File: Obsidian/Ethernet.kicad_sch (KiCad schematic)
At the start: 41 parts, among them J3 BELFUSE_0826-1G1T-43-F, U7 RTL8211F-CG, Y4 XTAL_25MHZ_EPSON_TSX-3225_25.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

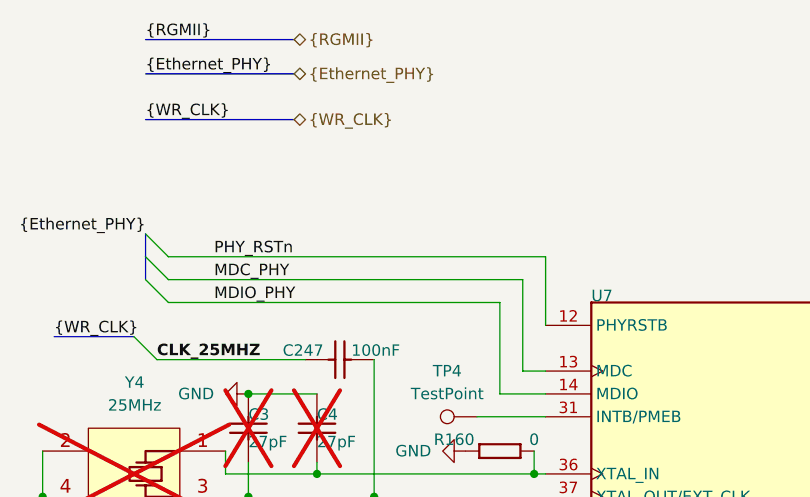
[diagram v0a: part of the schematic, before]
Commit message: adding lcsc reference for PMOD
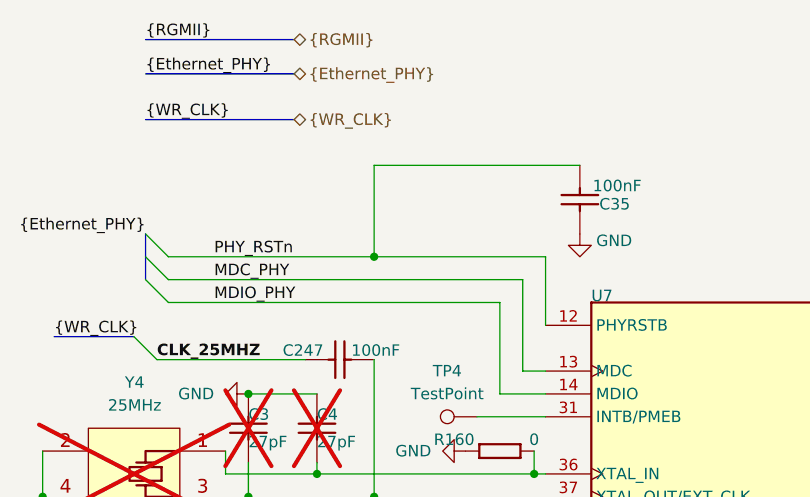
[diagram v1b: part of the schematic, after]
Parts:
- added C35: CC0402_100NF_50V_10%_X7R, Capacitor_SMD:C_0402_1005Metric, symbol Library_Symbol:CC0402_100NF_50V_10%_X7R
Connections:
- net GND: now also C35.2
- net PHY_RSTn: now also C35.1

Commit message: update LCSC reference, and OFFSET rotation for JLCPCB
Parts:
- C35: footprint Capacitor_SMD:C_0402_1005Metric -> Footprint:CAPC1005X55N
- J3: LCSC C6776261 -> C6062830
- L1: LCSC C6685204 -> C48945746
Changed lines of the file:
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@@
 			)
 		)
-		(property "Footprint" "Capacitor_SMD:C_0402_1005Metric"
+		(property "Footprint" "Footprint:CAPC1005X55N"
 			(at 73.152 34.29 0)
 			(effects
@@
 			)
 		)
-		(property "LCSC" "C6776261"
+		(property "LCSC" "C6062830"
 			(at 227.33 102.87 0)
 			(effects
@@
 			)
 		)
-		(property "LCSC" "C6685204"
+		(property "LCSC" "C48945746"
 			(at 157.48 77.47 0)
 			(effects

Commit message: update ethernet LCSC components
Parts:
- J3: Footprint Ref BEL_0826-1G1T-43-F -> 0826-1G1T-23-F; LCSC C6062830 -> C5467573
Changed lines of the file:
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@@
 			)
 		)
-		(property "Footprint Ref" "BEL_0826-1G1T-43-F"
+		(property "Footprint Ref" "0826-1G1T-23-F"
 			(at 227.33 15.875 0)
 			(effects
@@
 			)
 		)
-		(property "LCSC" "C6062830"
+		(property "LCSC" "C5467573"
 			(at 227.33 102.87 0)
 			(effects

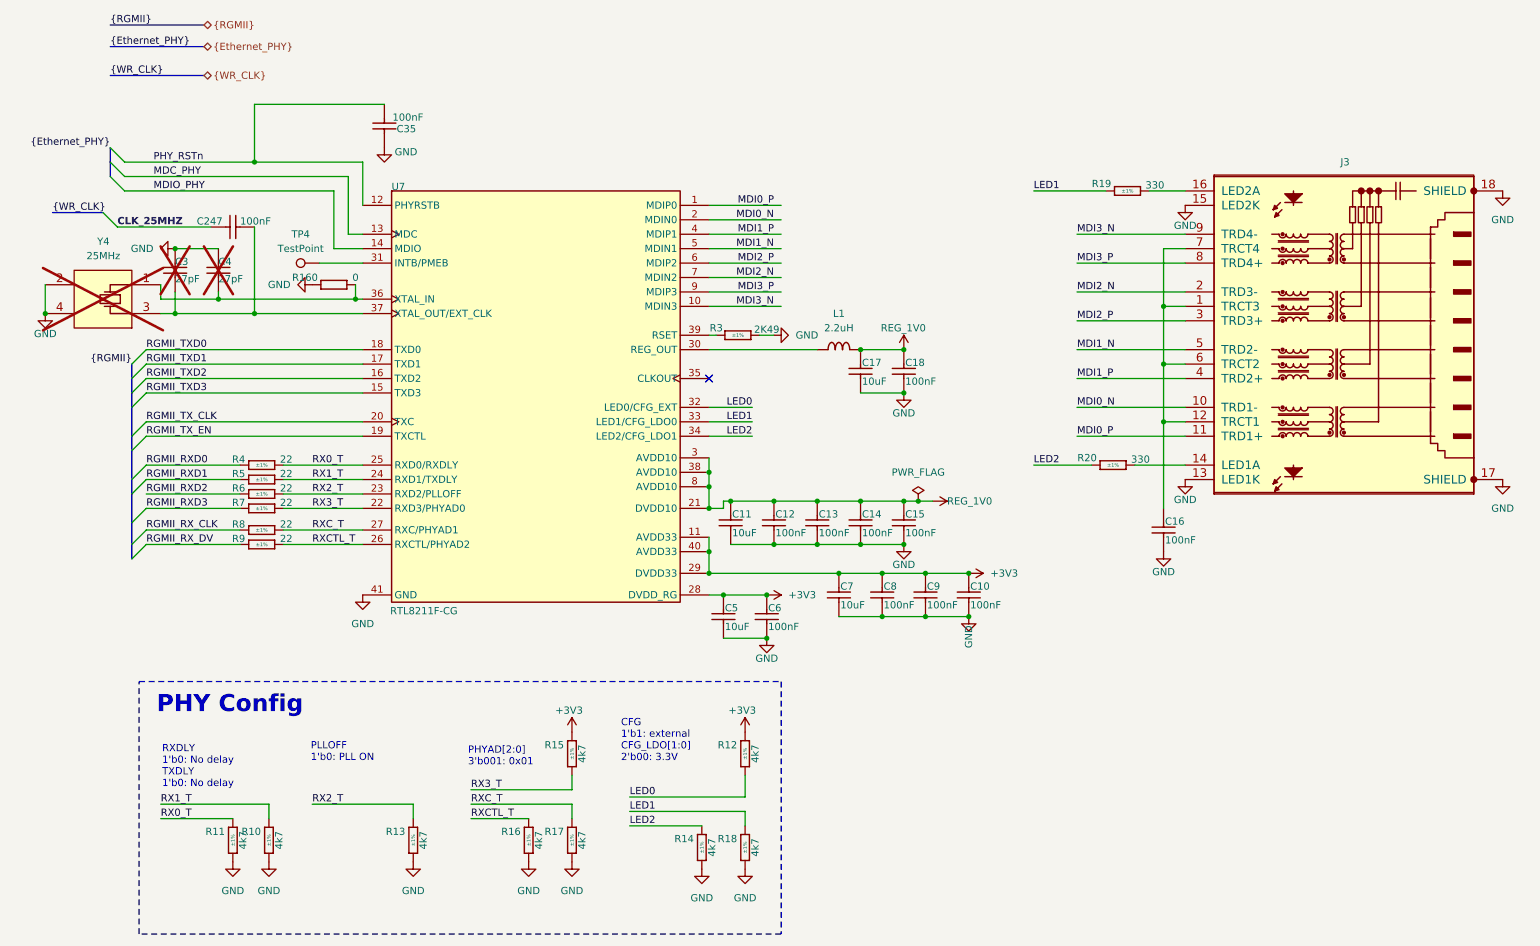
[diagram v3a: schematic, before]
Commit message: Cleaning symbol fields
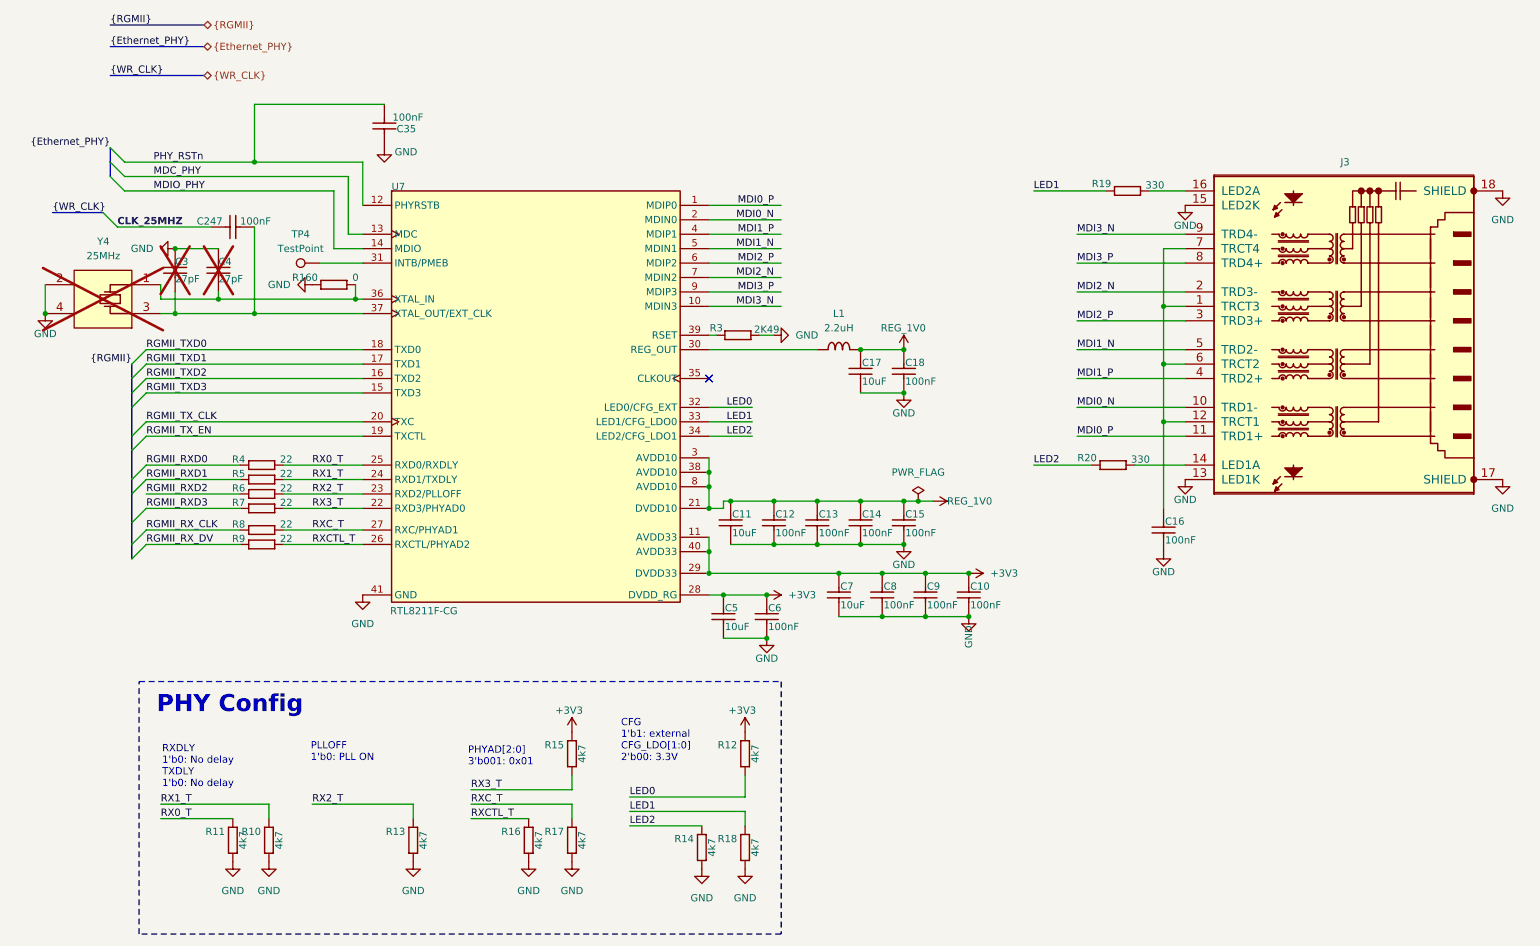
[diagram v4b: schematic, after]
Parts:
- C10, C12, C13, C14, C15, C16, C18, C247, C35, C6, C8, C9: Author CERN DEM MR -> (none); Case 0402 -> (none); Comment 100nF -> (none); Component Kind Standard -> (none); Component Type Standard -> (none); ComponentHeight (none) -> (none); CreateDate 06/30/17 00:00:00 -> (none); Database Table Name Capacitors -> (none); Footprint Library Capacitors SMD -> (none); Footprint Path PcbLib\Capacitors SMD.PcbLib -> (none); Footprint Ref CAPC1005X55N -> (none); HelpURL \\cern.ch\dfs\Applications\Altium\Datasheets\CC0402_MURATA_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 -> (none); LatestRevisionDate 06/30/17 00:00:00 -> (none); Library Name Capacitors SMD -> (none); Library Path SchLib\Capacitors.SchLib -> (none); Library Ref Capacitor - non polarized -> (none); License CC-BY-SA 4.0 -> (none); Manufacturer GENERIC -> (none); Manufacturer Part Number CC0402_100NF_50V_10%_X7R -> (none); Manufacturer1 ComponentHeight 0.55mm -> (none); Manufacturer1 Example MURATA -> (none); Manufacturer1 Part Number GRM155R71H104KE14D -> (none); Mounted Yes -> (none); PackageDescription (none) -> (none); Part Description SMD Multilayer Chip Ceramic Capacitor -> (none); Part Number CC0402_100NF_50V_10%_X7R -> (none); Pin Count 2 -> (none); PressFit (none) -> (none); SMD Yes -> (none); Sense No -> (none); Sense Comment (none) -> (none); Socket No -> (none); Status None -> (none); Status Comment (none) -> (none); TC X7R -> (none); Tolerance ±10% -> (none); Voltage 50V -> (none)
- C11, C17, C5, C7: Author CERN DEM JLC -> (none); Case 0402 -> (none); Comment 10uF -> (none); Component Kind Standard -> (none); Component Type Standard -> (none); ComponentHeight (none) -> (none); CreateDate 01/07/15 00:00:00 -> (none); Database Table Name Capacitors -> (none); Footprint Library Capacitors SMD -> (none); Footprint Path PcbLib\Capacitors SMD.PcbLib -> (none); Footprint Ref CAPC1005X70N -> (none); HelpURL \\cern.ch\dfs\Applications\Altium\Datasheets\CC0402_X5R_TDK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 -> (none); LatestRevisionDate 01/07/15 00:00:00 -> (none); Library Name Capacitors SMD -> (none); Library Path SchLib\Capacitors.SchLib -> (none); Library Ref Capacitor - non polarized -> (none); License CC-BY-SA 4.0 -> (none); Manufacturer GENERIC -> (none); Manufacturer Part Number CC0402_10UF_6.3V_20%_X5R -> (none); Manufacturer1 ComponentHeight 0.70mm -> (none); Manufacturer1 Example TDK -> (none); Manufacturer1 Part Number C1005X5R0J106M050 -> (none); Mounted Yes -> (none); PackageDescription (none) -> (none); Part Description SMD Multilayer Chip Ceramic Capacitor -> (none); Part Number CC0402_10UF_6.3V_20%_X5R -> (none); Pin Count 2 -> (none); PressFit (none) -> (none); SMD Yes -> (none); Sense No -> (none); Sense Comment (none) -> (none); Socket No -> (none); Status Preferred -> (none); Status Comment (none) -> (none); TC X5R -> (none); Tolerance ±10% -> (none); Voltage 6.3V -> (none)
- C3, C4: Author CERN DEM JLC -> (none); Case 0402 -> (none); Comment 27pF -> (none); Component Kind Standard -> (none); Component Type Standard -> (none); ComponentHeight (none) -> (none); CreateDate 10/25/12 00:00:00 -> (none); Database Table Name Capacitors -> (none); Footprint Library Capacitors SMD -> (none); Footprint Path PcbLib\Capacitors SMD.PcbLib -> (none); Footprint Ref CAPC1005X55N -> (none); HelpURL \\cern.ch\dfs\Applications\Altium\Datasheets\CC0402_C0G_KEM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 -> (none); LatestRevisionDate 04/22/15 00:00:00 -> (none); Library Name Capacitors SMD -> (none); Library Path SchLib\Capacitors.SchLib -> (none); Library Ref Capacitor - non polarized -> (none); License CC-BY-SA 4.0 -> (none); Manufacturer GENERIC -> (none); Manufacturer Part Number CC0402_27PF_50V_5%_C0G -> (none); Manufacturer1 ComponentHeight 0.55mm -> (none); Manufacturer1 Example KEMET -> (none); Manufacturer1 Part Number C0402C270J5GACTU -> (none); Mounted Yes -> (none); PackageDescription (none) -> (none); Part Description SMD Multilayer Chip Ceramic Capacitor -> (none); Part Number CC0402_27PF_50V_5%_C0G -> (none); Pin Count 2 -> (none); PressFit (none) -> (none); SMD Yes -> (none); Sense No -> (none); Sense Comment (none) -> (none); Socket No -> (none); Status Preferred -> (none); Status Comment (none) -> (none); TC C0G/NP0 -> (none); Tolerance ±5% -> (none); Voltage 50V -> (none)
- J3: Author CERN DEM JLC -> (none); Case (none) -> (none); Comment RJ45 -> (none); Component Kind Standard -> (none); Component Type Standard -> (none); ComponentHeight 13.61mm -> (none); ComponentLink1Description (none) -> (none); ComponentLink1URL (none) -> (none); ComponentLink2Description (none) -> (none); ComponentLink2URL (none) -> (none); CreateDate 12/02/10 00:00:00 -> (none); Database Table Name Connectors -> (none); Device (none) -> (none); Family RJ45 -> (none); Footprint Library Miscellaneous THD -> (none); Footprint Path PcbLib\Miscellaneous THD.PcbLib -> (none); Footprint Ref 0826-1G1T-23-F -> (none); HelpURL \\cern.ch\dfs\Applications\Altium\Datasheets\BEL_0826-1G1T-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 -> (none); LatestRevisionDate 09/20/18 00:00:00 -> (none); Library Name Miscellaneous -> (none); Library Path SchLib\Connectors.SchLib -> (none); Library Ref BEL_0826-1G1T-43-F -> (none); License CC-BY-SA 4.0 -> (none); Manufacturer BEL MAGNETIC SOLUTIONS -> (none); Manufacturer Part Number 0826-1G1T-43-F -> (none); Mounted Yes -> (none); PackageDescription (none) -> (none); Part Description 1 Port, Green/Green LEDs, RJ45 10/100/1000 Gigabit Ethernet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 -> (none); Part Number BELFUSE_0826-1G1T-43-F -> (none); Pin Count 18 -> (none); PressFit No -> (none); SCEM (none) -> (none); SMD No -> (none); Sense No -> (none); Sense Comment (none) -> (none); Socket No -> (none); Status None -> (none); Status Comment (none) -> (none)
- L1: Author CERN DEM HF -> (none); Case (none) -> (none); Comment 2.2uH -> (none); Component Kind Standard -> (none); Component Type Standard -> (none); ComponentHeight 1.2mm -> (none); CreateDate 06/23/22 00:00:00 -> (none); Database Table Name Inductors & Transformers -> (none); Footprint Library Inductors SMD -> (none); Footprint Path PcbLib\Inductors SMD.PcbLib -> (none); Footprint Ref IND_BOURNS_SRP3212 -> (none); HelpURL \\cern.ch\dfs\Applications\Altium\Datasheets\IND_BOURNS_SRP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 -> (none); LatestRevisionDate 06/23/22 00:00:00 -> (none); Library Name Inductors SMD -> (none); Library Path SchLib\Inductors & Transformers.SchLib -> (none); Library Ref Inductor -> (none); License CC-BY-SA 4.0 -> (none); Manufacturer BOURNS -> (none); Manufacturer Part Number SRP3212-2R2M -> (none); Mounted Yes -> (none); PackageDescription (none) -> (none); Part Description Shielded SMD Power Inductor -> (none); Part Number IND_2.2UH_20%_BOURNS_SRP3212 -> (none); Pin Count 2 -> (none); Power 4A -> (none); Resistance 0.061R -> (none); SMD Yes -> (none); Sense No -> (none); Sense Comment (none) -> (none); Socket No -> (none); Status (none) -> (none); Status Comment (none) -> (none); Tolerance ±20% -> (none)
- R10, R11, R12, R13, R14, R15, R16, R17, R18: Author CERN DEM JLC -> (none); Case 0402 -> (none); Comment 4k7 -> (none); Component Kind Standard -> (none); Component Type Standard -> (none); ComponentHeight (none) -> (none); CreateDate 12/03/07 00:00:00 -> (none); Database Table Name Resistors -> (none); Footprint Library Resistors SMD -> (none); Footprint Path PcbLib\Resistors SMD.PcbLib -> (none); Footprint Ref RESC1005X40N -> (none); HelpURL \\cern.ch\dfs\Applications\Altium\Datasheets\R0402_Phycomp_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 -> (none); LatestRevisionDate 10/17/12 00:00:00 -> (none); Library Name Resistors SMD -> (none); Library Path SchLib\Resistors.SchLib -> (none); Library Ref Resistor - 1% -> (none); License CC-BY-SA 4.0 -> (none); Manufacturer GENERIC -> (none); Manufacturer Part Number R0402_4K7_1%_0.0625W_100PPM -> (none); Manufacturer1 ComponentHeight 0.4mm -> (none); Manufacturer1 Example YAGEO PHYCOMP -> (none); Manufacturer1 Part Number 232270674702L -> (none); Mounted Yes -> (none); PackageDescription (none) -> (none); Part Description General Purpose Thick Film Chip Resistor -> (none); Part Number R0402_4K7_1%_0.0625W_100PPM -> (none); Pin Count 2 -> (none); Power 0.0625W -> (none); PressFit No -> (none); SMD Yes -> (none); Sense No -> (none); Sense Comment (none) -> (none); Socket No -> (none); Status Not Recommended -> (none); Status Comment (none) -> (none); TC ±100ppm/°C -> (none); Tolerance ±1% -> (none); Voltage (none) -> (none)
- R160: Case 0402 -> (none); Comment =Value -> (none); Component Kind Standard -> (none); Component Type Standard -> (none); ComponentHeight (none) -> (none); CreateDate 12/03/07 00:00:00 -> (none); Database Table Name Resistors -> (none); Footprint Library Resistors SMD -> (none); Footprint Path PcbLib\Resistors SMD.PcbLib -> (none); Footprint Ref RESC1005X40N -> (none); HelpURL \\cern.ch\dfs\Applications\Altium\Datasheets\R0402_Phycomp_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 -> (none); LatestRevisionDate 10/17/12 00:00:00 -> (none); Library Name Resistors SMD -> (none); Library Path SchLib\Resistors.SchLib -> (none); Library Ref Resistor -> (none); License This work is licensed under the Creative Commons CC-BY-SA 4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 -> (none); Manufacturer GENERIC -> (none); Manufacturer Part Number R0402_0R_JUMPER -> (none); Manufacturer1 ComponentHeight 0.4mm -> (none); Manufacturer1 Example YAGEO PHYCOMP -> (none); Manufacturer1 Part Number 232270591001L -> (none); Mounted Yes -> (none); PackageDescription (none) -> (none); Part Description 1A (0.05R Max DC Resistance) Zero Ohm Jumper -> (none); Part Number R0402_0R_JUMPER -> (none); Pin Count 2 -> (none); Power (none) -> (none); PressFit No -> (none); SMD Yes -> (none); Sense No -> (none); Sense Comment (none) -> (none); Socket No -> (none); Status Not Recommended -> (none); Status Comment (none) -> (none); TC (none) -> (none); Tolerance (none) -> (none); Voltage (none) -> (none)
- R19, R20: Author CERN DEM JLC -> (none); Case 0402 -> (none); Comment 330 -> (none); Component Kind Standard -> (none); Component Type Standard -> (none); ComponentHeight (none) -> (none); CreateDate 12/03/07 00:00:00 -> (none); Database Table Name Resistors -> (none); Footprint Library Resistors SMD -> (none); Footprint Path PcbLib\Resistors SMD.PcbLib -> (none); Footprint Ref RESC1005X40N -> (none); HelpURL \\cern.ch\dfs\Applications\Altium\Datasheets\R0402_Phycomp_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 -> (none); LatestRevisionDate 10/17/12 00:00:00 -> (none); Library Name Resistors SMD -> (none); Library Path SchLib\Resistors.SchLib -> (none); Library Ref Resistor - 1% -> (none); License CC-BY-SA 4.0 -> (none); Manufacturer GENERIC -> (none); Manufacturer Part Number R0402_330R_1%_0.0625W_100PPM -> (none); Manufacturer1 ComponentHeight 0.4mm -> (none); Manufacturer1 Example YAGEO PHYCOMP -> (none); Manufacturer1 Part Number 232270673301L -> (none); Mounted Yes -> (none); PackageDescription (none) -> (none); Part Description General Purpose Thick Film Chip Resistor -> (none); Part Number R0402_330R_1%_0.0625W_100PPM -> (none); Pin Count 2 -> (none); Power 0.0625W -> (none); PressFit No -> (none); SMD Yes -> (none); Sense No -> (none); Sense Comment (none) -> (none); Socket No -> (none); Status Not Recommended -> (none); Status Comment (none) -> (none); TC ±100ppm/°C -> (none); Tolerance ±1% -> (none); Voltage (none) -> (none)
- R3: Author CERN DEM BC -> (none); Case 0402 -> (none); Comment 2K49 -> (none); Component Kind Standard -> (none); Component Type Standard -> (none); ComponentHeight (none) -> (none); CreateDate 01/10/20 00:00:00 -> (none); Database Table Name Resistors -> (none); Footprint Library Resistors SMD -> (none); Footprint Path PcbLib\Resistors SMD.PcbLib -> (none); Footprint Ref RESC1005X40N -> (none); HelpURL \\cern.ch\dfs\Applications\Altium\Datasheets\R0402_VISHAY_C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 -> (none); LatestRevisionDate 01/10/20 00:00:00 -> (none); Library Name Resistors SMD -> (none); Library Path SchLib\Resistors.SchLib -> (none); Library Ref Resistor - 1% -> (none); License CC-BY-SA 4.0 -> (none); Manufacturer GENERIC -> (none); Manufacturer Part Number R0402_2K49_1%_0.063W_100PPM -> (none); Manufacturer1 ComponentHeight 0.4mm -> (none); Manufacturer1 Example VISHAY -> (none); Manufacturer1 Part Number CRCW04022K49FK -> (none); Mounted Yes -> (none); PackageDescription (none) -> (none); Part Description General Purpose Thick Film Chip Resistor -> (none); Part Number R0402_2K49_1%_0.063W_100PPM -> (none); Pin Count 2 -> (none); Power 0.063W -> (none); PressFit No -> (none); SMD Yes -> (none); Sense No -> (none); Sense Comment (none) -> (none); Socket No -> (none); Status None -> (none); Status Comment (none) -> (none); TC ±100ppm/°C -> (none); Tolerance ±1% -> (none); Voltage (none) -> (none)
- R4, R5, R6, R7, R8, R9: Author CERN DEM JLC -> (none); Case 0402 -> (none); Comment 22 -> (none); Component Kind Standard -> (none); Component Type Standard -> (none); ComponentHeight (none) -> (none); CreateDate 12/03/07 00:00:00 -> (none); Database Table Name Resistors -> (none); Footprint Library Resistors SMD -> (none); Footprint Path PcbLib\Resistors SMD.PcbLib -> (none); Footprint Ref RESC1005X40N -> (none); HelpURL \\cern.ch\dfs\Applications\Altium\Datasheets\R0402_Phycomp_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 -> (none); LatestRevisionDate 10/17/12 00:00:00 -> (none); Library Name Resistors SMD -> (none); Library Path SchLib\Resistors.SchLib -> (none); Library Ref Resistor - 1% -> (none); License CC-BY-SA 4.0 -> (none); Manufacturer GENERIC -> (none); Manufacturer Part Number R0402_22R_1%_0.0625W_100PPM -> (none); Manufacturer1 ComponentHeight 0.4mm -> (none); Manufacturer1 Example YAGEO PHYCOMP -> (none); Manufacturer1 Part Number 232270672209L -> (none); Mounted Yes -> (none); PackageDescription (none) -> (none); Part Description General Purpose Thick Film Chip Resistor -> (none); Part Number R0402_22R_1%_0.0625W_100PPM -> (none); Pin Count 2 -> (none); Power 0.0625W -> (none); PressFit No -> (none); SMD Yes -> (none); Sense No -> (none); Sense Comment (none) -> (none); Socket No -> (none); Status Not Recommended -> (none); Status Comment (none) -> (none); TC ±100ppm/°C -> (none); Tolerance ±1% -> (none); Voltage (none) -> (none)
- U7: ALTIUM_VALUE * -> (none); CHECK_PRICES https://www.snapeda.com/parts/RTL8211F-CG/Realtek/view-part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 -> (none); MF Realtek Semiconductor Corp -> (none); MP RTL8211F-CG -> (none); PACKAGE None -> (none); SNAPEDA_LINK https://www.snapeda.com/parts/RTL8211F-CG/Realtek/view-part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 -> (none)
- Y4: Author CERN DEM JLC -> (none); Bonding No -> (none); Case (none) -> (none); Comment 25MHz -> (none); Component Kind Standard -> (none); Component Type Standard -> (none); ComponentHeight 0.6mm -> (none); ComponentLink1Description Ordering Informations -> (none); ComponentLink1URL \\cern.ch\dfs\Applications\Altium\Datasheets\XTAL_EPSON_TSX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 -> (none); ComponentLink2Description (none) -> (none); ComponentLink2URL (none) -> (none); CreateDate 04/03/12 00:00:00 -> (none); Database Table Name ICs And Semiconductors -> (none); Device (none) -> (none); Footprint Library ICs And Semiconductors SMD -> (none); Footprint Path PcbLib\ICs And Semiconductors SMD.PcbLib -> (none); Footprint Ref XTAL_EPSON_TSX-3225 -> (none); HelpURL \\cern.ch\dfs\Applications\Altium\Datasheets\XTAL_EPSON_TSX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 -> (none); LatestRevisionDate 10/06/16 00:00:00 -> (none); Library Name Crystals & Oscillators -> (none); Library Path SchLib\Crystals & Oscillators.SchLib -> (none); Library Ref Quartz Crystal 1X 2GND 3X 4GND -> (none); License CC-BY-SA 4.0 -> (none); Manufacturer EPSON -> (none); Manufacturer Part Number TSX-3225 25.0000MF10Z-AC -> (none); Mounted Yes -> (none); PackageDescription Crystal, Corner Concave; 4 Pin, 2.50mm L X 3.20mm W X 0.6mm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 -> (none); Part Description Tolerance: ±10ppm, Stability:±10ppm, -20°C to 75°C, 9pF, Su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 -> (none); Part Number XTAL_25MHZ_EPSON_TSX-3225_25.0000MF10Z-AC -> (none); Pin Count 4 -> (none); PressFit No -> (none); SMD Yes -> (none); Sense No -> (none); Sense Comment (none) -> (none); Socket No -> (none); Status (none) -> (none); Status Comment (none) -> (none)

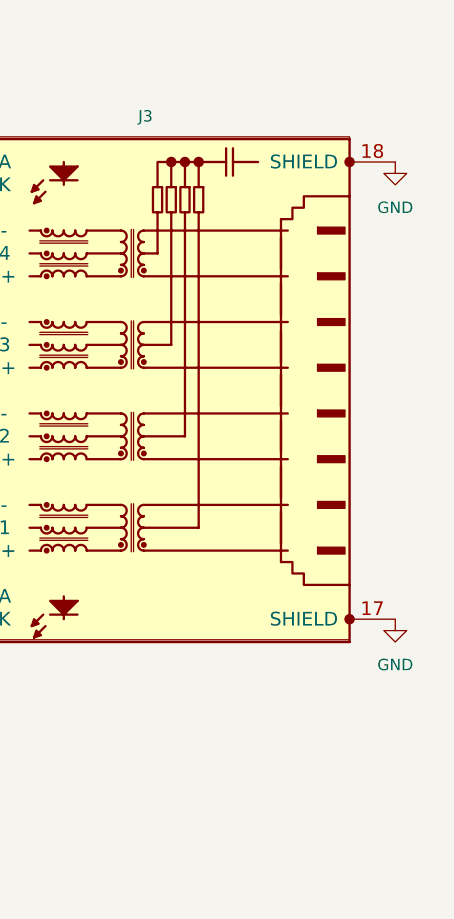
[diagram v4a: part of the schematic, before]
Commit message: Adding the gnd shield
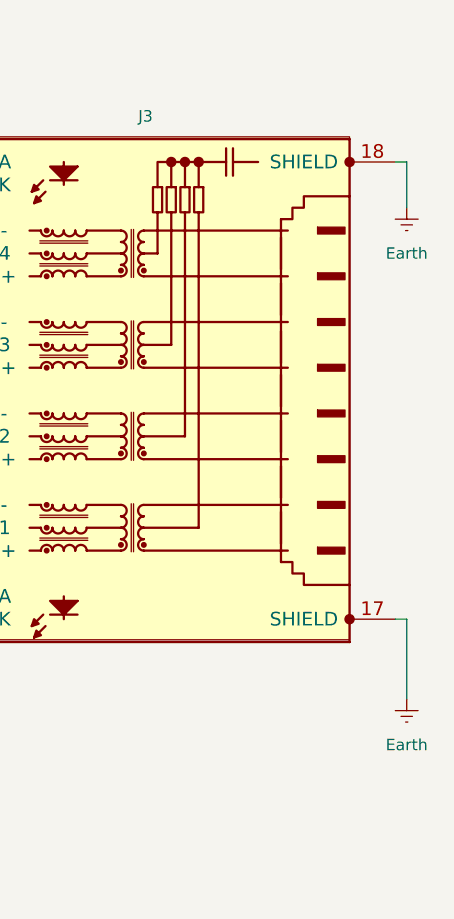
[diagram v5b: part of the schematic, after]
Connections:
- net GND: no longer J3.17 (SHIELD), J3.18 (SHIELD)
- new net Earth: J3.17 (SHIELD), J3.18 (SHIELD)
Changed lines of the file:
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@@
 		)
 	)
+	(wire
+		(pts
+			(xy 278.13 49.53) (xy 279.4 49.53)
+		)
+		(stroke
+			(width 0)
+			(type default)
+		)
+	)
 	(bus
 		(pts
@@
 	(wire
 		(pts
+			(xy 279.4 49.53) (xy 279.4 54.61)
+		)
+		(stroke
+			(width 0)
+			(type default)
+		)
+	)
+	(wire
+		(pts
 			(xy 41.91 160.02) (xy 54.61 160.02)
 		)
@@
 		)
 	)
+	(wire
+		(pts
+			(xy 279.4 100.33) (xy 279.4 109.22)
+		)
+		(stroke
+			(width 0)
+			(type default)
+		)
+	)
 	(bus
 		(pts
@@
 	(wire
 		(pts
+			(xy 279.4 100.33) (xy 278.13 100.33)
+		)
+		(stroke
+			(width 0)
+			(type default)
+		)
+	)
+	(wire
+		(pts
 			(xy 39.37 97.79) (xy 55.88 97.79)
 		)
@@
 	)
 	(symbol
-		(lib_id "Library_Symbol:GND")
-		(at 54.61 167.64 0)
+		(lib_id "power:Earth")
+		(at 279.4 54.61 0)
 		(unit 1)
 		(exclude_from_sim no)
@@
 		(dnp no)
 		(fields_autoplaced yes)
-		(property "Reference" "#PWR022"
-			(at 54.61 173.99 0)
+		(property "Reference" "#PWR012"
+			(at 279.4 60.96 0)
 			(effects
 				(font
@@
 			)
 		)
-		(property "Value" "GND"
-			(at 54.61 172.72 0)
+		(property "Value" "Earth"
+			(at 279.4 59.69 0)
 			(effects
 				(font
@@
 		)
 		(property "Footprint" ""
-			(at 54.61 167.64 0)
+			(at 279.4 54.61 0)
 			(effects
 				(font
@@
 			)
 		)
-		(property "Datasheet" ""
-			(at 54.61 167.64 0)
+		(property "Datasheet" "~"
+			(at 279.4 54.61 0)
 			(effects
 				(font
@@
 			)
 		)
-		(property "Description" "Power symbol creates a global label with name \"GND\" , ground"
-			(at 54.61 167.64 0)
+		(property "Description" "Power symbol creates a global label with name \"Earth\""
+			(at 279.4 54.61 0)
 			(effects
 				(font
@@
 		)
 		(instances
-			(project "Marble_Tiny"
+			(project ""
 				(path "/c2a4f786-b14c-434a-acf7-b20fb2221b0b/41baefe0-2999-4159-91c6-ae67dbf0b6a8"
-					(reference "#PWR022")
+					(reference "#PWR012")
 					(unit 1)
 				)
@@
 	(symbol
 		(lib_id "Library_Symbol:GND")
-		(at 278.13 49.53 0)
+		(at 54.61 167.64 0)
 		(unit 1)
 		(exclude_from_sim no)
@@
 		(dnp no)
 		(fields_autoplaced yes)
-		(property "Reference" "#PWR012"
-			(at 278.13 55.88 0)
+		(property "Reference" "#PWR022"
+			(at 54.61 173.99 0)
 			(effects
 				(font
@@
 		)
 		(property "Value" "GND"
-			(at 278.13 54.61 0)
+			(at 54.61 172.72 0)
 			(effects
 				(font
@@
 		)
 		(property "Footprint" ""
-			(at 278.13 49.53 0)
+			(at 54.61 167.64 0)
 			(effects
 				(font
@@
 		)
 		(property "Datasheet" ""
-			(at 278.13 49.53 0)
+			(at 54.61 167.64 0)
 			(effects
 				(font
@@
 		)
 		(property "Description" "Power symbol creates a global label with name \"GND\" , ground"
-			(at 278.13 49.53 0)
+			(at 54.61 167.64 0)
 			(effects
 				(font
@@
 			(project "Marble_Tiny"
 				(path "/c2a4f786-b14c-434a-acf7-b20fb2221b0b/41baefe0-2999-4159-91c6-ae67dbf0b6a8"
-					(reference "#PWR012")
+					(reference "#PWR022")
 					(unit 1)
 				)
@@
 	)
 	(symbol
-		(lib_id "Library_Symbol:GND")
-		(at 278.13 100.33 0)
-		(unit 1)
-		(exclude_from_sim no)
-		(in_bom yes)
-		(on_board yes)
-		(dnp no)
-		(fields_autoplaced yes)
-		(property "Reference" "#PWR011"
-			(at 278.13 106.68 0)
-			(effects
-				(font
-					(size 1.27 1.27)
-				)
-				(hide yes)
-			)
-		)
-		(property "Value" "GND"
-			(at 278.13 105.41 0)
-			(effects
-				(font
-					(size 1.27 1.27)
-				)
-			)
-		)
-		(property "Footprint" ""
-			(at 278.13 100.33 0)
-			(effects
-				(font
-					(size 1.27 1.27)
-				)
-				(hide yes)
-			)
-		)
-		(property "Datasheet" ""
-			(at 278.13 100.33 0)
-			(effects
-				(font
-					(size 1.27 1.27)
-				)
-				(hide yes)
-			)
-		)
-		(property "Description" "Power symbol creates a global label with name \"GND\" , ground"
-			(at 278.13 100.33 0)
-			(effects
-				(font
-					(size 1.27 1.27)
-				)
-				(hide yes)
-			)
-		)
-		(pin "1"
-		)
-		(instances
-			(project "Marble_Tiny"
-				(path "/c2a4f786-b14c-434a-acf7-b20fb2221b0b/41baefe0-2999-4159-91c6-ae67dbf0b6a8"
-					(reference "#PWR011")
-					(unit 1)
-				)
-			)
-		)
-	)
-	(symbol
 		(lib_id "Library_Symbol:R0402_22R_1%_0.0625W_100PPM")
 		(at 55.88 102.87 0)
@@
 					(unit 1)
 				)
+			)
+		)
+	)
+	(symbol
+		(lib_id "power:Earth")
+		(at 279.4 109.22 0)
+		(unit 1)
+		(exclude_from_sim no)
+		(in_bom yes)
+		(on_board yes)
+		(dnp no)
+		(fields_autoplaced yes)
+		(property "Reference" "#PWR011"
+			(at 279.4 115.57 0)
+			(effects
+				(font
+					(size 1.27 1.27)
+				)
+				(hide yes)
+			)
+		)
+		(property "Value" "Earth"
+			(at 279.4 114.3 0)
+			(effects
+				(font
+					(size 1.27 1.27)
+				)
+			)
+		)
+		(property "Footprint" ""
+			(at 279.4 109.22 0)
+			(effects
+				(font
+					(size 1.27 1.27)
+				)
+				(hide yes)
+			)
+		)
+		(property "Datasheet" "~"
+			(at 279.4 109.22 0)
+			(effects
+				(font
+					(size 1.27 1.27)
+				)
+				(hide yes)
+			)
+		)
+		(property "Description" "Power symbol creates a global label with name \"Earth\""
+			(at 279.4 109.22 0)
+			(effects
+				(font
+					(size 1.27 1.27)
+				)
+				(hide yes)
+			)
+		)
+		(pin "1"
+		)
+		(instances
+			(project "Obsidian"
+				(path "/c2a4f786-b14c-434a-acf7-b20fb2221b0b/41baefe0-2999-4159-91c6-ae67dbf0b6a8"
+					(reference "#PWR011")
+					(unit 1)
+				)
